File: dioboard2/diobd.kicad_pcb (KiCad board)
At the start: 2 copper layers, 58.4 x 15.2 mm, 9 parts, among them J1 Conn_01x03, J2 Conn_01x03, J3 Conn_01x03, J4 Conn_01x03

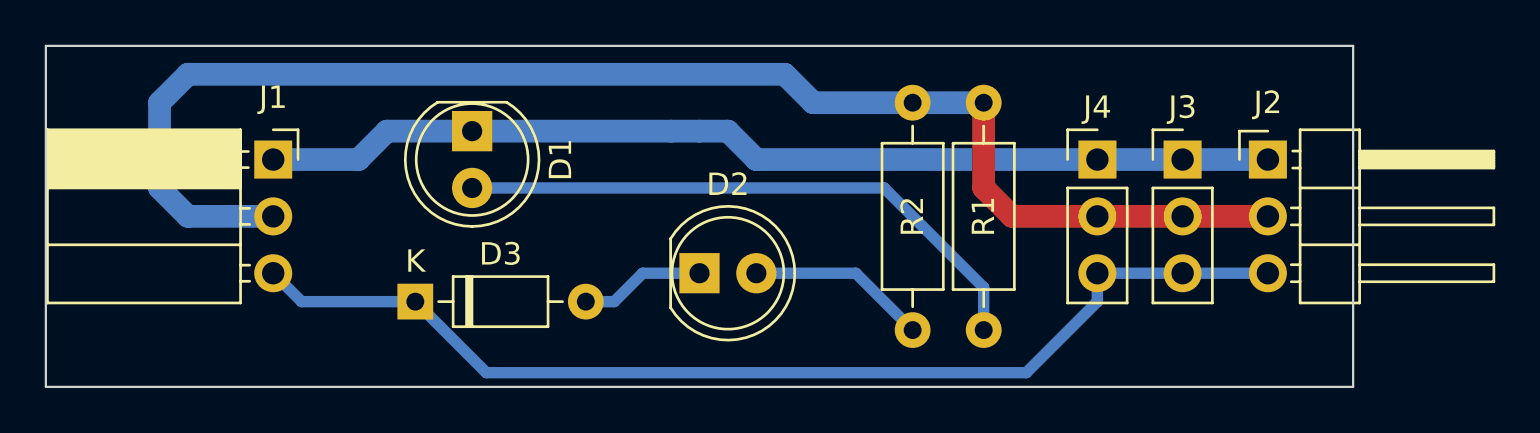
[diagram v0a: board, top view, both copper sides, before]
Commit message: delete traces so we can practice routing fix .gitignore for pcb backup files
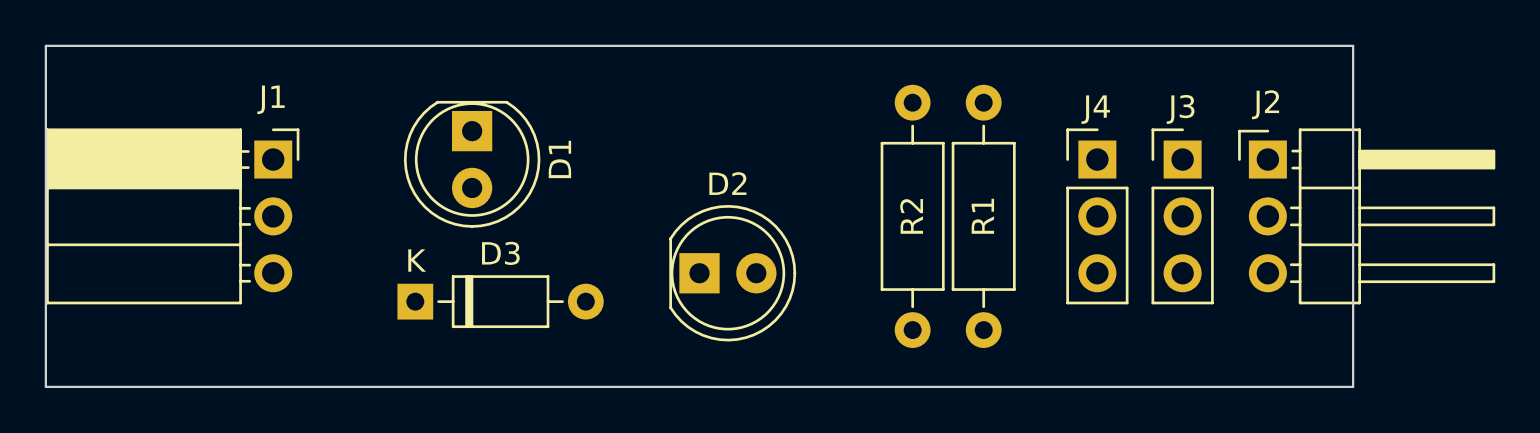
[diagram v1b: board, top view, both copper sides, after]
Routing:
- net +5V: track 64.3 -> 0.00 mm
- net /signal: track 48.9 -> 0.00 mm
- net Earth: track 45.5 -> 0.00 mm
- net Net-(D1-Pad2): track 26.6 -> 0.00 mm
- net Net-(D2-Pad2): track 8.04 -> 0.00 mm
- net Net-(D2-Pad1): track 5.61 -> 0.00 mm
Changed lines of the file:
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@@
-(kicad_pcb (version 20171130) (host pcbnew 5.0.0)
+(kicad_pcb (version 20171130) (host pcbnew 5.0.1-33cea8e~68~ubuntu16.04.1)
   (general
     (thickness 1.5748)
     (drawings 4)
-    (tracks 33)
+    (tracks 0)
     (zones 0)
     (modules 9)
@@
   )
   (setup
-    (last_trace_width 0.508)
+    (last_trace_width 0.2032)
     (user_trace_width 0.254)
     (user_trace_width 0.508)
@@
     (pad_drill 0.6)
     (pad_to_mask_clearance 0)
+    (solder_mask_min_width 0.25)
     (aux_axis_origin 0 0)
     (grid_origin 93.98 102.87)
@@
   (gr_line (start 152.4 102.87) (end 152.4 87.63) (layer Edge.Cuts) (width 0.1))
   (gr_line (start 93.98 102.87) (end 152.4 102.87) (layer Edge.Cuts) (width 0.1))
-  (segment (start 135.89 100.33) (end 135.89 98.425) (width 0.508) (layer B.Cu) (net 1))
-  (segment (start 131.445 93.98) (end 113.03 93.98) (width 0.508) (layer B.Cu) (net 1))
-  (segment (start 135.89 98.425) (end 131.445 93.98) (width 0.508) (layer B.Cu) (net 1))
-  (segment (start 104.14 92.71) (end 107.95 92.71) (width 1.016) (layer B.Cu) (net 2))
-  (segment (start 109.22 91.44) (end 113.03 91.44) (width 1.016) (layer B.Cu) (net 2))
-  (segment (start 107.95 92.71) (end 109.22 91.44) (width 1.016) (layer B.Cu) (net 2))
-  (segment (start 125.73 92.71) (end 148.59 92.71) (width 1.016) (layer B.Cu) (net 2))
-  (segment (start 113.03 91.44) (end 121.92 91.44) (width 1.016) (layer B.Cu) (net 2))
-  (segment (start 121.92 91.44) (end 123.19 91.44) (width 1.016) (layer B.Cu) (net 2))
-  (segment (start 123.19 91.44) (end 124.46 91.44) (width 1.016) (layer B.Cu) (net 2))
-  (segment (start 124.46 91.44) (end 125.73 92.71) (width 1.016) (layer B.Cu) (net 2))
-  (segment (start 118.11 99.06) (end 119.38 99.06) (width 0.508) (layer B.Cu) (net 3))
-  (segment (start 120.65 97.79) (end 123.19 97.79) (width 0.508) (layer B.Cu) (net 3))
-  (segment (start 119.38 99.06) (end 120.65 97.79) (width 0.508) (layer B.Cu) (net 3))
-  (segment (start 130.175 97.79) (end 132.715 100.33) (width 0.508) (layer B.Cu) (net 4))
-  (segment (start 125.73 97.79) (end 130.175 97.79) (width 0.508) (layer B.Cu) (net 4))
-  (segment (start 148.59 97.79) (end 140.97 97.79) (width 0.508) (layer B.Cu) (net 5))
-  (segment (start 113.665 102.235) (end 110.49 99.06) (width 0.508) (layer B.Cu) (net 5))
-  (segment (start 137.795 102.235) (end 113.665 102.235) (width 0.508) (layer B.Cu) (net 5))
-  (segment (start 140.97 99.06) (end 137.795 102.235) (width 0.508) (layer B.Cu) (net 5))
-  (segment (start 140.97 97.79) (end 140.97 99.06) (width 0.508) (layer B.Cu) (net 5))
-  (segment (start 105.41 99.06) (end 104.14 97.79) (width 0.508) (layer B.Cu) (net 5))
-  (segment (start 110.49 99.06) (end 105.41 99.06) (width 0.508) (layer B.Cu) (net 5))
-  (segment (start 128.27 90.17) (end 135.89 90.17) (width 1.016) (layer B.Cu) (net 6))
-  (segment (start 127 88.9) (end 128.27 90.17) (width 1.016) (layer B.Cu) (net 6))
-  (segment (start 100.33 88.9) (end 127 88.9) (width 1.016) (layer B.Cu) (net 6))
-  (segment (start 104.14 95.25) (end 100.33 95.25) (width 1.016) (layer B.Cu) (net 6))
-  (segment (start 99.06 93.98) (end 99.06 90.17) (width 1.016) (layer B.Cu) (net 6))
-  (segment (start 100.33 95.25) (end 99.06 93.98) (width 1.016) (layer B.Cu) (net 6))
-  (segment (start 99.06 90.17) (end 100.33 88.9) (width 1.016) (layer B.Cu) (net 6))
-  (segment (start 137.16 95.25) (end 135.89 93.98) (width 1.016) (layer F.Cu) (net 6))
-  (segment (start 135.89 93.98) (end 135.89 90.17) (width 1.016) (layer F.Cu) (net 6))
-  (segment (start 148.59 95.25) (end 137.16 95.25) (width 1.016) (layer F.Cu) (net 6))
 )

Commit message: made pcb more compact
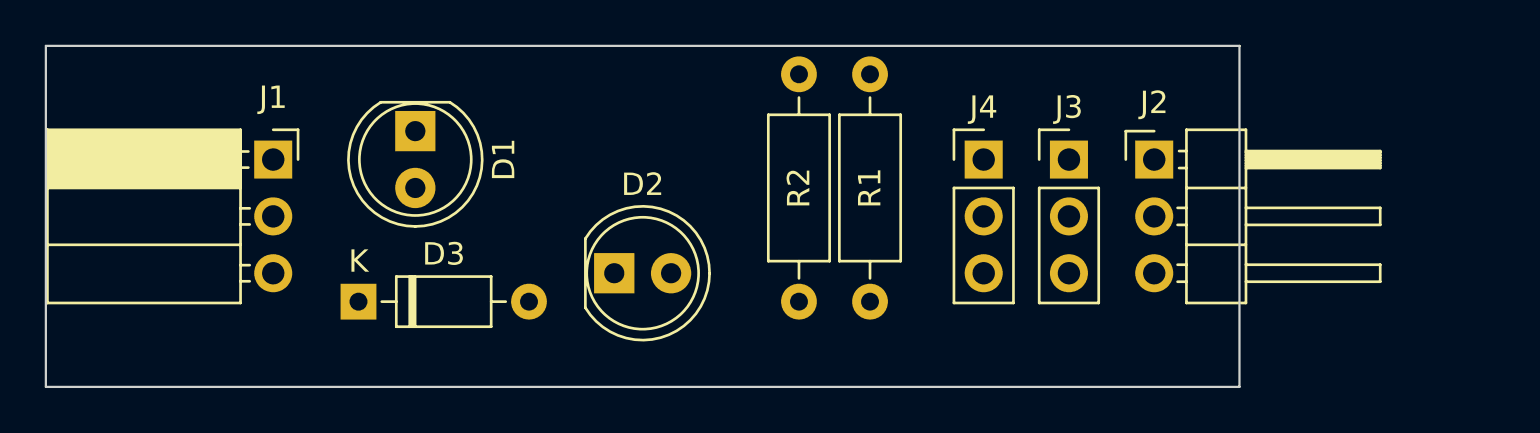
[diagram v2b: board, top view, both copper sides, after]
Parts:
- moved R2 5.24 mm to (127.6, 88.9)
- moved R1 5.24 mm to (130.8, 88.9)
- moved J2 5.08 mm to (143.5, 92.7)
- moved J3 5.08 mm to (139.7, 92.7)
- moved J4 5.08 mm to (135.9, 92.7)
- moved D2 3.81 mm to (119.4, 97.8)
- moved D1 2.54 mm to (110.5, 91.4)
- moved D3 2.54 mm to (108.0, 99.1)
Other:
- board size 58.4 x 15.2 mm -> 53.3 x 15.2 mm
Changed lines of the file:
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@@
-(kicad_pcb (version 20171130) (host pcbnew 5.0.1-33cea8e~68~ubuntu16.04.1)
+(kicad_pcb (version 20171130) (host pcbnew "(5.0.1)-3")
   (general
     (thickness 1.5748)
@@
     (aux_axis_origin 0 0)
     (grid_origin 93.98 102.87)
-    (visible_elements FFFFFF7F)
+    (visible_elements 7FFFFFFF)
     (pcbplotparams
       (layerselection 0x010fc_ffffffff)
@@
   )
   (module LED_THT:LED_D5.0mm (layer F.Cu)
-    (at 113.03 91.44 270)
+    (at 110.49 91.44 270)
     (descr "LED, diameter 5.0mm, 2 pins, http://cdn-reichelt.de/documents/datenblatt/A500/LL-504BC2E-009.pdf")
     (tags "LED diameter 5.0mm 2 pins")
@@
   )
   (module LED_THT:LED_D5.0mm (layer F.Cu)
-    (at 123.19 97.79)
+    (at 119.38 97.79)
     (descr "LED, diameter 5.0mm, 2 pins, http://cdn-reichelt.de/documents/datenblatt/A500/LL-504BC2E-009.pdf")
     (tags "LED diameter 5.0mm 2 pins")
@@
   )
   (module Diode_THT:D_DO-35_SOD27_P7.62mm_Horizontal (layer F.Cu)
-    (at 110.49 99.06)
+    (at 107.95 99.06)
     (descr "Diode, DO-35_SOD27 series, Axial, Horizontal, pin pitch=7.62mm, , length*diameter=4*2mm^2, , http://www.diodes.com/_files/packages/DO-35.pdf")
     (tags "Diode DO-35_SOD27 series Axial Horizontal pin pitch 7.62mm  length 4mm diameter 2mm")
@@
   )
   (module Connector_PinHeader_2.54mm:PinHeader_1x03_P2.54mm_Horizontal (layer F.Cu)
-    (at 148.59 92.71)
+    (at 143.51 92.71)
     (descr "Through hole angled pin header, 1x03, 2.54mm pitch, 6mm pin length, single row")
     (tags "Through hole angled pin header THT 1x03 2.54mm single row")
@@
   )
   (module Connector_PinHeader_2.54mm:PinHeader_1x03_P2.54mm_Vertical (layer F.Cu)
-    (at 144.78 92.71)
+    (at 139.7 92.71)
     (descr "Through hole straight pin header, 1x03, 2.54mm pitch, single row")
     (tags "Through hole pin header THT 1x03 2.54mm single row")
@@
   )
   (module Connector_PinHeader_2.54mm:PinHeader_1x03_P2.54mm_Vertical (layer F.Cu)
-    (at 140.97 92.71)
+    (at 135.89 92.71)
     (descr "Through hole straight pin header, 1x03, 2.54mm pitch, single row")
     (tags "Through hole pin header THT 1x03 2.54mm single row")
@@
   )
   (module Resistor_THT:R_Axial_DIN0207_L6.3mm_D2.5mm_P10.16mm_Horizontal (layer F.Cu)
-    (at 135.89 90.17 270)
+    (at 130.81 88.9 270)
     (descr "Resistor, Axial_DIN0207 series, Axial, Horizontal, pin pitch=10.16mm, 0.25W = 1/4W, length*diameter=6.3*2.5mm^2, http://cdn-reichelt.de/documents/datenblatt/B400/1_4W%23YAG.pdf")
     (tags "Resistor Axial_DIN0207 series Axial Horizontal pin pitch 10.16mm 0.25W = 1/4W length 6.3mm diameter 2.5mm")
@@
   )
   (module Resistor_THT:R_Axial_DIN0207_L6.3mm_D2.5mm_P10.16mm_Horizontal (layer F.Cu)
-    (at 132.715 90.17 270)
+    (at 127.635 88.9 270)
     (descr "Resistor, Axial_DIN0207 series, Axial, Horizontal, pin pitch=10.16mm, 0.25W = 1/4W, length*diameter=6.3*2.5mm^2, http://cdn-reichelt.de/documents/datenblatt/B400/1_4W%23YAG.pdf")
     (tags "Resistor Axial_DIN0207 series Axial Horizontal pin pitch 10.16mm 0.25W = 1/4W length 6.3mm diameter 2.5mm")
@@
   )
   (gr_line (start 93.98 87.63) (end 93.98 102.87) (layer Edge.Cuts) (width 0.1))
-  (gr_line (start 152.4 87.63) (end 93.98 87.63) (layer Edge.Cuts) (width 0.1))
-  (gr_line (start 152.4 102.87) (end 152.4 87.63) (layer Edge.Cuts) (width 0.1))
-  (gr_line (start 93.98 102.87) (end 152.4 102.87) (layer Edge.Cuts) (width 0.1))
+  (gr_line (start 147.32 87.63) (end 93.98 87.63) (layer Edge.Cuts) (width 0.1))
+  (gr_line (start 147.32 102.87) (end 147.32 87.63) (layer Edge.Cuts) (width 0.1))
+  (gr_line (start 93.98 102.87) (end 147.32 102.87) (layer Edge.Cuts) (width 0.1))
 )

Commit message: Resolve Merge Error
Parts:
- moved R2 5.24 mm to (132.7, 90.2)
- moved R1 5.24 mm to (135.9, 90.2)
- moved J2 5.08 mm to (148.6, 92.7)
- moved J3 5.08 mm to (144.8, 92.7)
- moved J4 5.08 mm to (141.0, 92.7)
- moved D2 3.81 mm to (123.2, 97.8)
- moved D1 2.54 mm to (113.0, 91.4)
- moved D3 2.54 mm to (110.5, 99.1)
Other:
- board size 53.3 x 15.2 mm -> 58.4 x 15.2 mm
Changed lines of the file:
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@@
-(kicad_pcb (version 20171130) (host pcbnew "(5.0.1)-3")
+(kicad_pcb (version 20171130) (host pcbnew 5.0.1-33cea8e~68~ubuntu16.04.1)
   (general
     (thickness 1.5748)
@@
     (aux_axis_origin 0 0)
     (grid_origin 93.98 102.87)
-    (visible_elements 7FFFFFFF)
+    (visible_elements FFFFFF7F)
     (pcbplotparams
       (layerselection 0x010fc_ffffffff)
@@
   )
   (module LED_THT:LED_D5.0mm (layer F.Cu)
-    (at 110.49 91.44 270)
+    (at 113.03 91.44 270)
     (descr "LED, diameter 5.0mm, 2 pins, http://cdn-reichelt.de/documents/datenblatt/A500/LL-504BC2E-009.pdf")
     (tags "LED diameter 5.0mm 2 pins")
@@
   )
   (module LED_THT:LED_D5.0mm (layer F.Cu)
-    (at 119.38 97.79)
+    (at 123.19 97.79)
     (descr "LED, diameter 5.0mm, 2 pins, http://cdn-reichelt.de/documents/datenblatt/A500/LL-504BC2E-009.pdf")
     (tags "LED diameter 5.0mm 2 pins")
@@
   )
   (module Diode_THT:D_DO-35_SOD27_P7.62mm_Horizontal (layer F.Cu)
-    (at 107.95 99.06)
+    (at 110.49 99.06)
     (descr "Diode, DO-35_SOD27 series, Axial, Horizontal, pin pitch=7.62mm, , length*diameter=4*2mm^2, , http://www.diodes.com/_files/packages/DO-35.pdf")
     (tags "Diode DO-35_SOD27 series Axial Horizontal pin pitch 7.62mm  length 4mm diameter 2mm")
@@
   )
   (module Connector_PinHeader_2.54mm:PinHeader_1x03_P2.54mm_Horizontal (layer F.Cu)
-    (at 143.51 92.71)
+    (at 148.59 92.71)
     (descr "Through hole angled pin header, 1x03, 2.54mm pitch, 6mm pin length, single row")
     (tags "Through hole angled pin header THT 1x03 2.54mm single row")
@@
   )
   (module Connector_PinHeader_2.54mm:PinHeader_1x03_P2.54mm_Vertical (layer F.Cu)
-    (at 139.7 92.71)
+    (at 144.78 92.71)
     (descr "Through hole straight pin header, 1x03, 2.54mm pitch, single row")
     (tags "Through hole pin header THT 1x03 2.54mm single row")
@@
   )
   (module Connector_PinHeader_2.54mm:PinHeader_1x03_P2.54mm_Vertical (layer F.Cu)
-    (at 135.89 92.71)
+    (at 140.97 92.71)
     (descr "Through hole straight pin header, 1x03, 2.54mm pitch, single row")
     (tags "Through hole pin header THT 1x03 2.54mm single row")
@@
   )
   (module Resistor_THT:R_Axial_DIN0207_L6.3mm_D2.5mm_P10.16mm_Horizontal (layer F.Cu)
-    (at 130.81 88.9 270)
+    (at 135.89 90.17 270)
     (descr "Resistor, Axial_DIN0207 series, Axial, Horizontal, pin pitch=10.16mm, 0.25W = 1/4W, length*diameter=6.3*2.5mm^2, http://cdn-reichelt.de/documents/datenblatt/B400/1_4W%23YAG.pdf")
     (tags "Resistor Axial_DIN0207 series Axial Horizontal pin pitch 10.16mm 0.25W = 1/4W length 6.3mm diameter 2.5mm")
@@
   )
   (module Resistor_THT:R_Axial_DIN0207_L6.3mm_D2.5mm_P10.16mm_Horizontal (layer F.Cu)
-    (at 127.635 88.9 270)
+    (at 132.715 90.17 270)
     (descr "Resistor, Axial_DIN0207 series, Axial, Horizontal, pin pitch=10.16mm, 0.25W = 1/4W, length*diameter=6.3*2.5mm^2, http://cdn-reichelt.de/documents/datenblatt/B400/1_4W%23YAG.pdf")
     (tags "Resistor Axial_DIN0207 series Axial Horizontal pin pitch 10.16mm 0.25W = 1/4W length 6.3mm diameter 2.5mm")
@@
   )
   (gr_line (start 93.98 87.63) (end 93.98 102.87) (layer Edge.Cuts) (width 0.1))
-  (gr_line (start 147.32 87.63) (end 93.98 87.63) (layer Edge.Cuts) (width 0.1))
-  (gr_line (start 147.32 102.87) (end 147.32 87.63) (layer Edge.Cuts) (width 0.1))
-  (gr_line (start 93.98 102.87) (end 147.32 102.87) (layer Edge.Cuts) (width 0.1))
+  (gr_line (start 152.4 87.63) (end 93.98 87.63) (layer Edge.Cuts) (width 0.1))
+  (gr_line (start 152.4 102.87) (end 152.4 87.63) (layer Edge.Cuts) (width 0.1))
+  (gr_line (start 93.98 102.87) (end 152.4 102.87) (layer Edge.Cuts) (width 0.1))
 )
